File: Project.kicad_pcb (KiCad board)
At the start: 2 copper layers, 64.8 x 54.6 mm, 61 parts, among them J1 Power terminal, J2 Conn_01x24_Pin, J3 LED_pins, Q1 BC857, Q2 BC857, Q3 BC857, Q4 BC857, Q5 BC857, Q6 BC857, Q7 BC857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

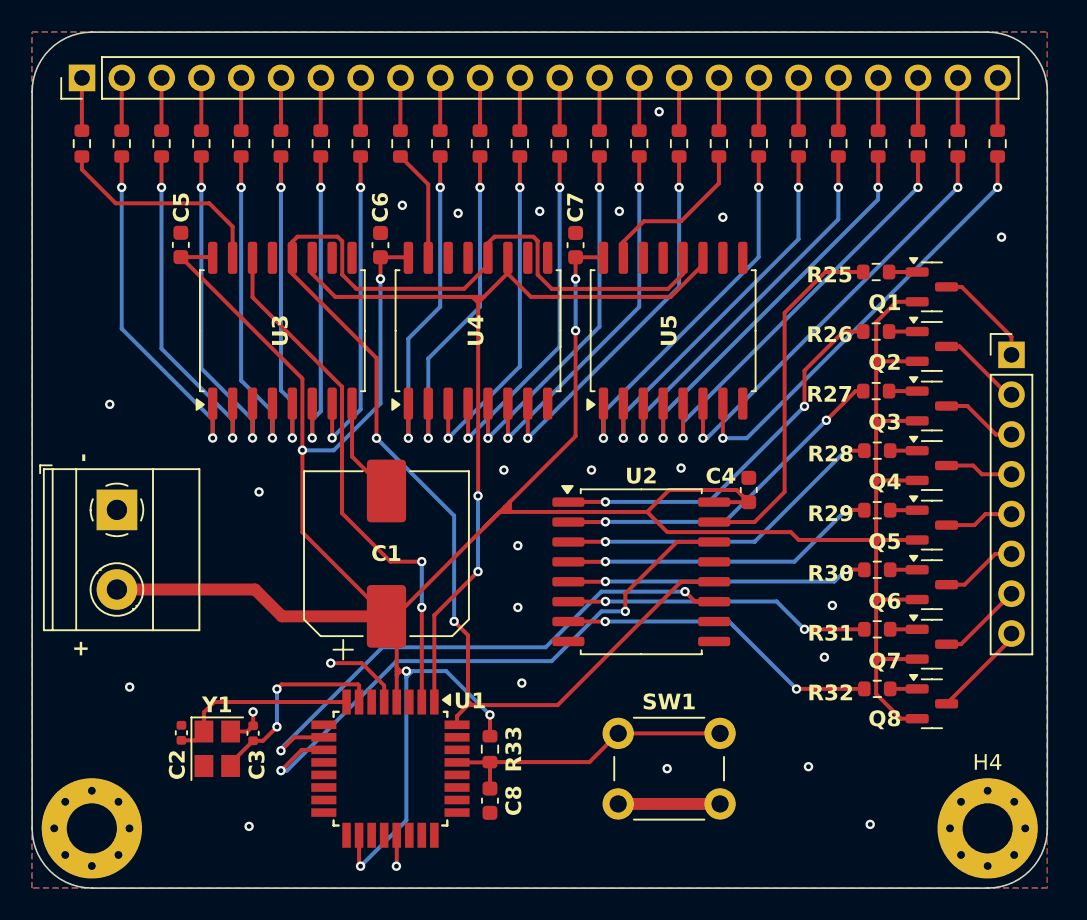
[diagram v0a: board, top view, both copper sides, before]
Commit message: PCB design done, BOM still undecided
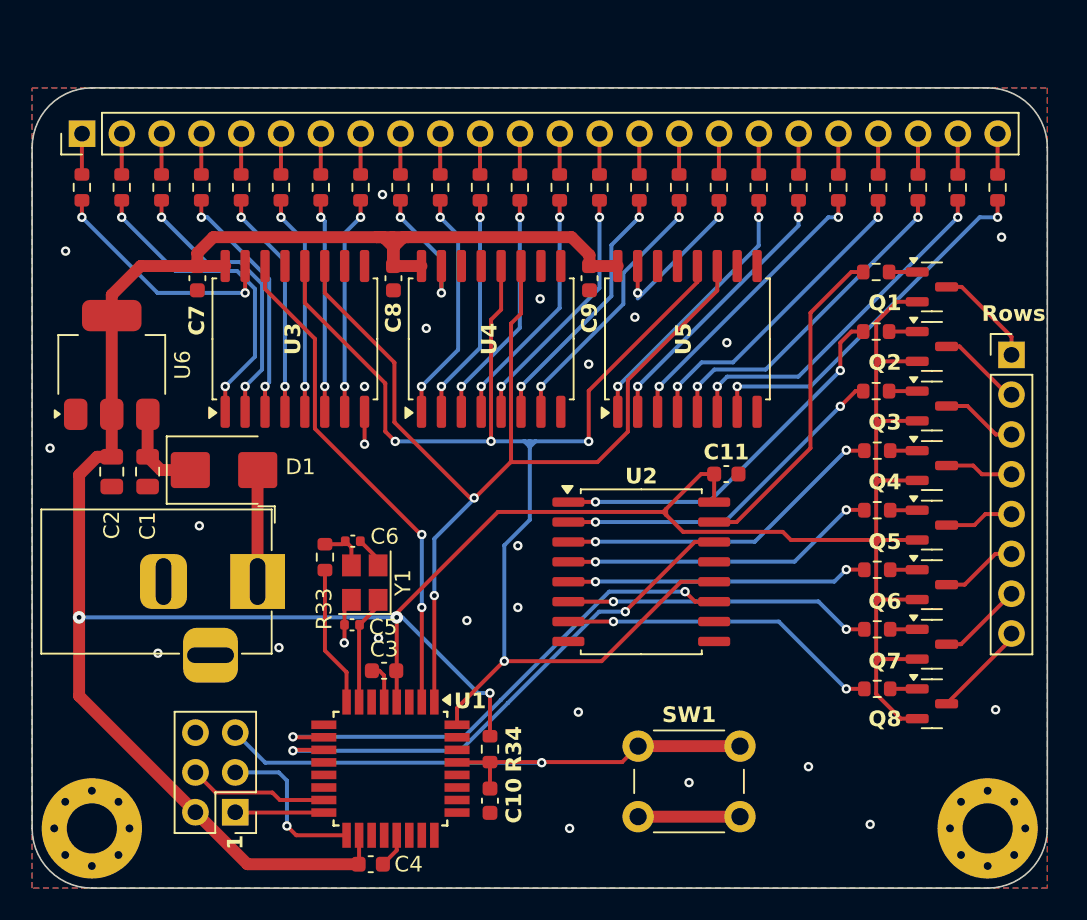
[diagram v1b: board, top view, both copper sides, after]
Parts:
- removed H3, H4: MountingHole_Pad, MountingHole:MountingHole_3.2mm_M3_Pad_Via
- added 1: ICSP_Connector, Connector_PinHeader_2.54mm:PinHeader_2x03_P2.54mm_Vertical, F.Cu at (114.6, 134.9)
- added C4: 100nF, Capacitor_SMD:C_0603_1608Metric, F.Cu at (123.2, 138.2)
- added C5: 22p, Capacitor_SMD:C_0402_1005Metric, F.Cu at (122.0, 122.9)
- added C6: 22p, Capacitor_SMD:C_0402_1005Metric, F.Cu at (122.1, 117.6)
- added D1: M7, Diode_SMD:D_SMB, F.Cu at (113.8, 113.0)
- added H1: MountingHole_Pad, MountingHole:MountingHole_3.2mm_M3_Pad_Via, F.Cu at (105.4, 135.9)
- added H2: MountingHole_Pad, MountingHole:MountingHole_3.2mm_M3_Pad_Via, F.Cu at (162.6, 135.9)
- added R33: 47R, Resistor_SMD:R_0603_1608Metric, F.Cu at (120.3, 118.6)
- added U6: AMS1117-5.0, Package_TO_SOT_SMD:SOT-223-3_TabPin2, F.Cu at (106.7, 106.3)
- C1: value 220uF -> 10uF; footprint Capacitor_SMD:CP_Elec_10x10 -> Capacitor_SMD:C_0805_2012Metric
- C2: value 22p -> 10uF; footprint Capacitor_SMD:C_0402_1005Metric -> Capacitor_SMD:C_0805_2012Metric
- C3: value 22p -> 100nF; footprint Capacitor_SMD:C_0402_1005Metric -> Capacitor_SMD:C_0603_1608Metric
- J1: value Power terminal -> DC Jack; footprint TerminalBlock_Phoenix:TerminalBlock_Phoenix_MKDS-1,5-2-5.08_1x02_P5.08mm_Horizontal -> Connector_BarrelJack:BarrelJack_Horizontal
- J2: value Conn_01x24_Pin -> LED_Cols
- J3: value LED_pins -> LED_Rows
- moved C2 17.2 mm to (106.7, 113.1), turned to -90 degrees
- moved C1 16.1 mm to (109.0, 113.1), turned to -90 degrees
- moved Y1 14.2 mm to (122.8, 120.2), turned to 90 degrees
- moved J1 10.1 mm to (116.0, 120.1), turned to 0 degrees
- moved C3 9.26 mm to (124.1, 125.8), turned to 180 degrees
- moved J2 3.56 mm to (104.8, 91.6)
- moved R1 2.79 mm to (104.8, 95.0)
- moved R10 2.79 mm to (127.6, 95.0)
- moved R11 2.79 mm to (130.2, 95.0)
- moved R12 2.79 mm to (132.7, 95.0)
- moved R13 2.79 mm to (135.3, 95.0)
- moved R14 2.79 mm to (137.8, 95.0)
- moved R15 2.79 mm to (140.3, 95.0)
- moved R16 2.79 mm to (142.9, 95.0)
- moved R17 2.79 mm to (145.4, 95.0)
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- renumbered C8 to C10, C4 to C11, C5 to C7, C6 to C8, C7 to C9, R33 to R34
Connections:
- net /MCU_pin12 renamed /D6
- net /MCU_pin13 renamed /D7
- net /MCU_pin4 renamed /D2
- net /MCU_pin5 renamed /D3
- net /MCU_pin6 renamed /D4
- net Net-(U1-~{RESET}/PC6) renamed NRST
- C1 pad 1: +5V -> Net-(D1-K)
- C2 pad 1: Net-(U1-XTAL2/PB7) -> +5V
- C3 pad 1: Net-(U1-XTAL1/PB6) -> +5V
- J1 pad 1: GND -> /Digital Headers/Vin
- J1 pad 2: +5V -> GND
- U1 pad 15: unconnected-(U1-PB3-Pad15) -> MOSI0
- U1 pad 16: unconnected-(U1-PB4-Pad16) -> MISO0
- U1 pad 17: unconnected-(U1-PB5-Pad17) -> SCK0
- U1 pad 7: Net-(U1-XTAL1/PB6) -> XTAL1
- U1 pad 8: Net-(U1-XTAL2/PB7) -> XTAL2
- Y1 pad 1: Net-(U1-XTAL2/PB7) -> XTAL1
- Y1 pad 3: Net-(U1-XTAL1/PB6) -> Net-(C6-Pad1)
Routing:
- net NRST: track 19.2 -> 40.5 mm, vias 0 -> 1
- net Net-(U1-XTAL1/PB6): track 12.8 -> 0.00 mm, vias 2 -> 0
- net Net-(U1-XTAL2/PB7): track 12.3 -> 0.00 mm
- net /D3: track 58.7 -> 70.2 mm
- net SCK0: track 0.00 -> 10.5 mm, vias 0 -> 1
- net +5V: track 213.2 -> 222.8 mm, vias 7 -> 3
- net XTAL2: track 0.00 -> 8.99 mm
- net MOSI0: track 0.00 -> 8.92 mm
- net /Digital Headers/Vin: track 0.00 -> 7.82 mm
- net Net-(U4-QF): track 23.1 -> 15.9 mm
- net Net-(U3-QH): track 21.0 -> 13.9 mm
- net Net-(U4-QE): track 22.6 -> 15.5 mm
- net Net-(U5-QB): track 24.3 -> 17.2 mm
- net Net-(U5-QC): track 24.8 -> 17.8 mm
- net Net-(U4-QH): track 24.2 -> 17.2 mm
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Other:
- board size 64.8 x 54.6 mm -> 64.8 x 51.1 mm
- board text added: "Rows"
- board text removed: "+"
- board text removed: "-"

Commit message: 595 column chip not daisy chained and  floating OE pins mistakes corrected
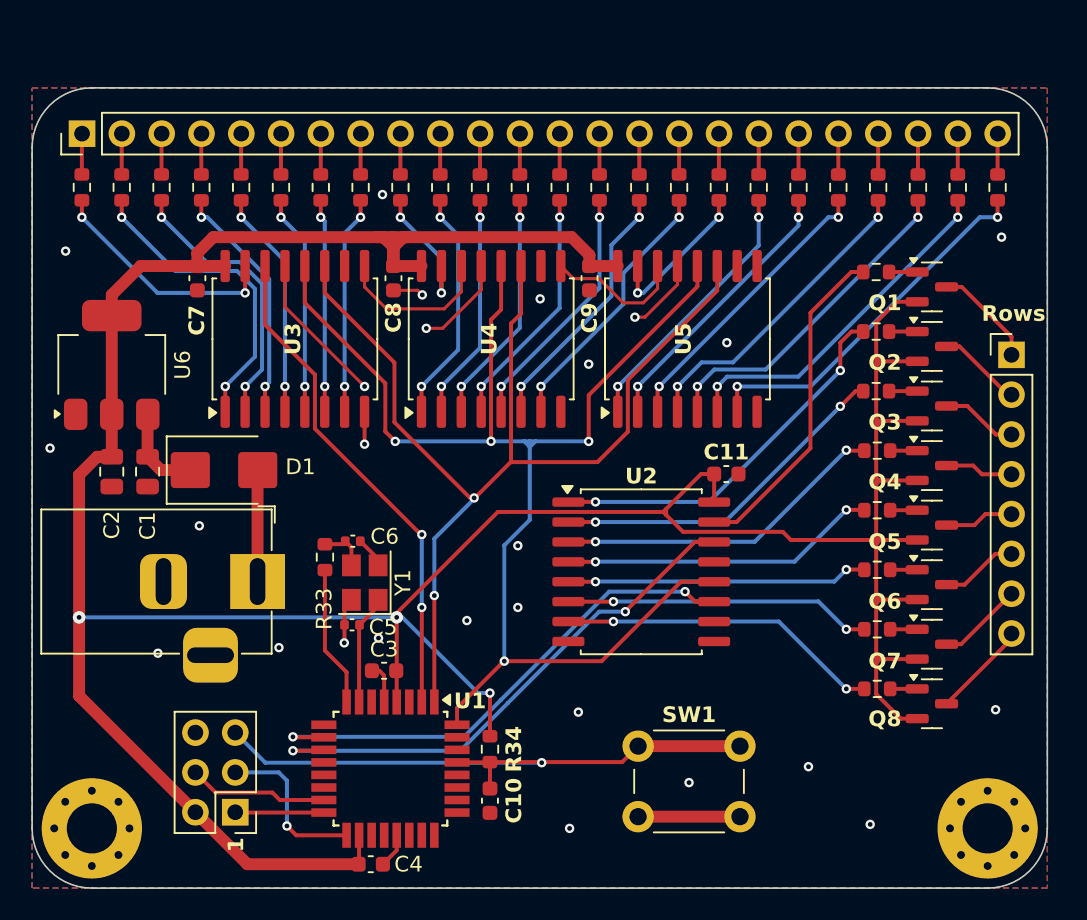
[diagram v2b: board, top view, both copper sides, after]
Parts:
- R1, R10, R11, R12, R13, R14, R15, R16, R17, R18, R19, R2, R20, R21, R22, R23, R24, R3, R4, R5, R6, R7, R8, R9: value 100R -> 220R
- renumbered 1 to J4
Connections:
- net /D2 renamed /RCLK
- net /D3 renamed /Col_Latch
- net /D4 renamed /Col_Data
- net /D6 renamed /Row_Latch
- net /D7 renamed /Row_Data
- net /Digital Headers/Vin renamed /Columns and DC Jack/Vin
- U2 pad 13: unconnected-(U2-~{OE}-Pad13) -> GND
- U3 pad 13: unconnected-(U3-~{OE}-Pad13) -> GND
- U3 pad 9: unconnected-(U3-QH'-Pad9) -> /QH'1
- U4 pad 13: unconnected-(U4-~{OE}-Pad13) -> GND
- U4 pad 14: unconnected-(U4-SER-Pad14) -> /QH'1
- U4 pad 9: unconnected-(U4-QH'-Pad9) -> /QH'2
- U5 pad 13: unconnected-(U5-~{OE}-Pad13) -> GND
- U5 pad 14: unconnected-(U5-SER-Pad14) -> /QH'2
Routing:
- net GND: track 17.3 -> 39.8 mm, vias 25 -> 26
- net /QH'1: track 0.00 -> 10.2 mm
- net /QH'2: track 0.00 -> 8.96 mm
- net /Columns and DC Jack/Vin: track 7.82 -> 7.05 mm
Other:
- board text added: "1"
